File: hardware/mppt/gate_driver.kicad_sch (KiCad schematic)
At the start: 26 parts, among them Q1001 BSS127S, U1001 ADUM4221-1ARIZ

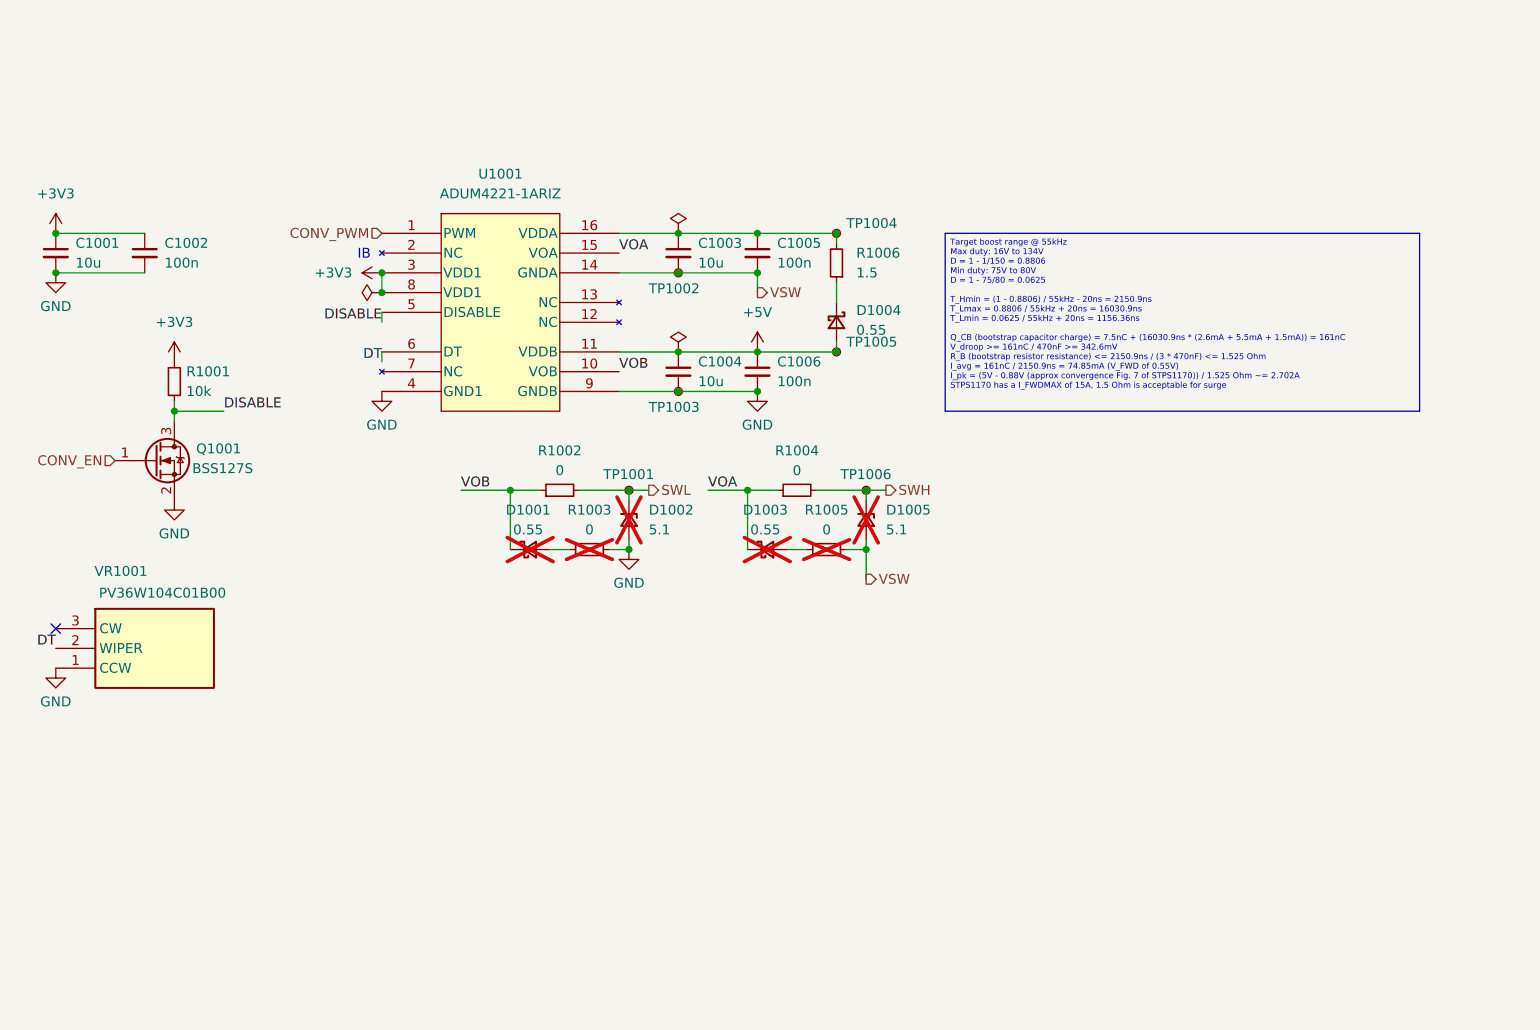
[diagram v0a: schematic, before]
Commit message: run through mppt sch, going through bom
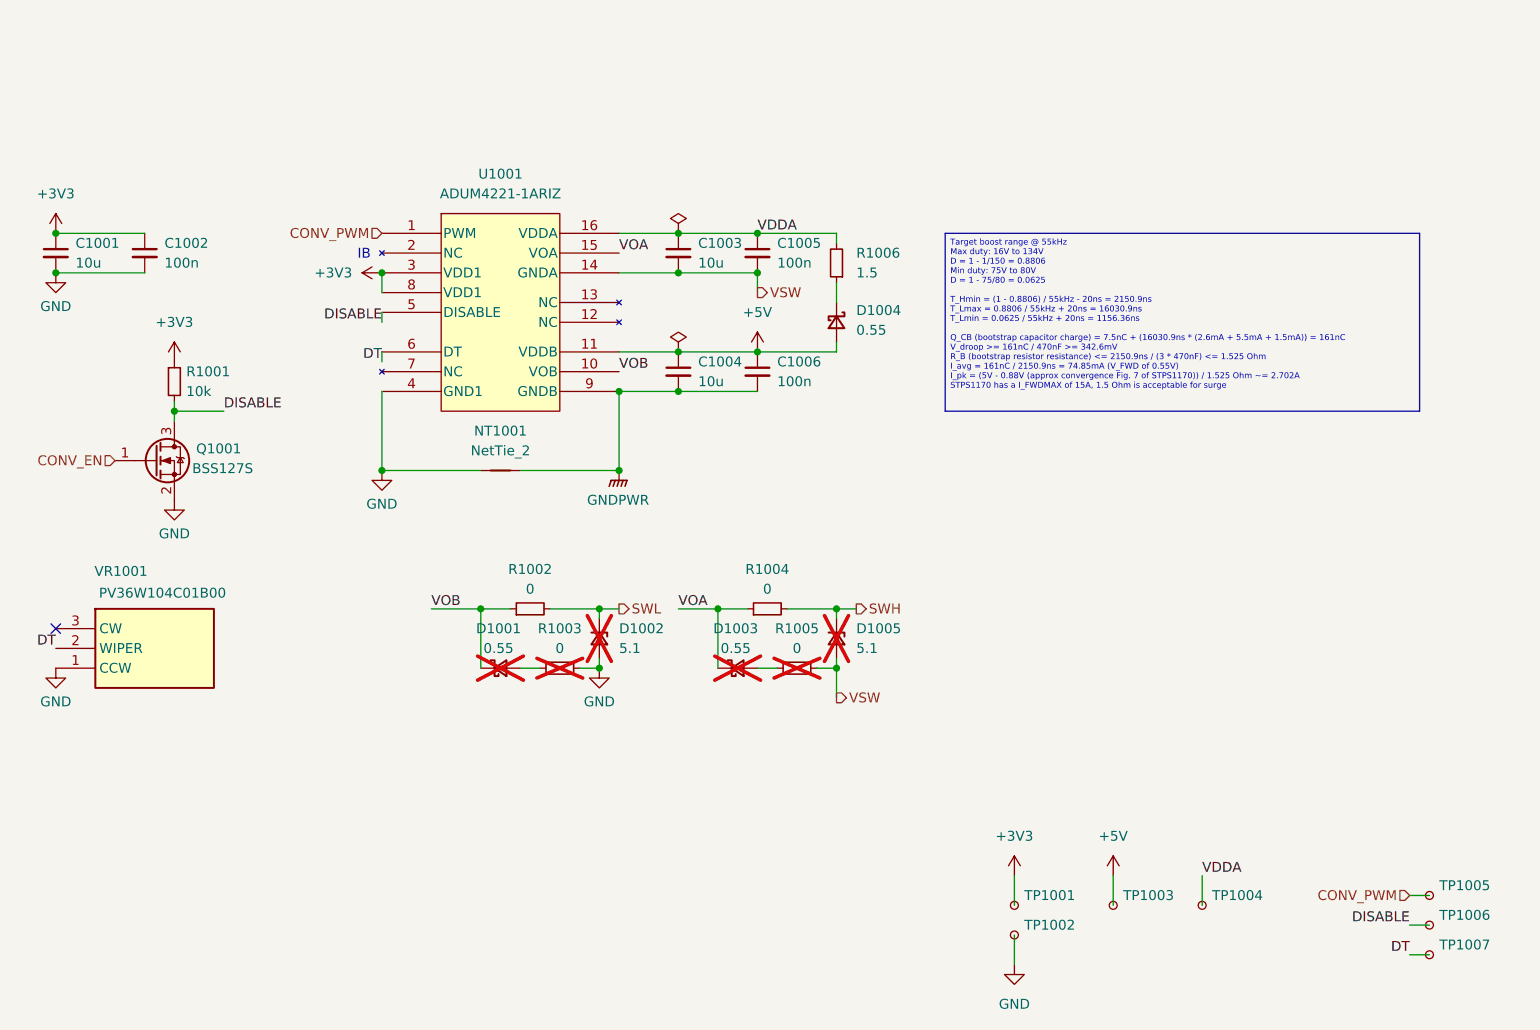
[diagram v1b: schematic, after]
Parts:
- added NT1001: NetTie_2, symbol Device:NetTie_2
- added TP1007: TestPoint_Small, symbol Connector:TestPoint_Small
- C1001: footprint Capacitor_SMD:C_0805_2012Metric_Pad1.18x1.45mm_HandSolder -> (none); Notes (none) -> 3.3V Rating; P/N CL21B106KOQNNNE -> (none)
- C1002: footprint Capacitor_SMD:C_0805_2012Metric_Pad1.18x1.45mm_HandSolder -> (none); Notes (none) -> 3.3V Rating; P/N CL21B104KCFNNNE -> (none)
- C1003, C1004: footprint Capacitor_SMD:C_0805_2012Metric_Pad1.18x1.45mm_HandSolder -> (none); Notes (none) -> 10V Rating; P/N CL21B106KOQNNNE -> (none)
- C1005, C1006: footprint Capacitor_SMD:C_0805_2012Metric_Pad1.18x1.45mm_HandSolder -> (none); Notes (none) -> 10V Rating; P/N CL21B104KCFNNNE -> (none)
- D1001, D1003, D1004: footprint footprints:stm_STPS1170AF -> (none); Manufacturer STMicrolectronics -> (none); P/N STPS1170AF -> (none)
- D1002, D1005: footprint Diode_SMD:D_SOD-123 -> (none); Manufacturer Vishay Electronics -> (none); P/N BZT52C5V1-G3-08 -> (none)
- Q1001: footprint Package_TO_SOT_SMD:SOT-23 -> (none); Manufacturer Diodes Incorporated -> (none); P/N BSS127S-7 -> (none)
- R1001: footprint Resistor_SMD:R_0805_2012Metric_Pad1.20x1.40mm_HandSolder -> (none); P/N CRCW080510K0FKEA -> (none)
- R1002, R1003, R1004, R1005: footprint Resistor_SMD:R_0805_2012Metric_Pad1.20x1.40mm_HandSolder -> (none); P/N CRCW08050000Z0EA -> (none)
- R1006: footprint Resistor_SMD:R_0805_2012Metric_Pad1.20x1.40mm_HandSolder -> (none); P/N CRCW08051R50FKEA -> (none)
- TP1001, TP1002: footprint TestPoint:TestPoint_Keystone_5000-5004_Miniature -> TestPoint:TestPoint_Pad_D1.0mm; Manufacturer Keystone Electronics -> (none); P/N 5000 -> (none)
- TP1003, TP1004, TP1005, TP1006: footprint TestPoint:TestPoint_Keystone_5000-5004_Miniature -> (none); Manufacturer Keystone Electronics -> (none); P/N 5000 -> (none)
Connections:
- net +3V3: now also TP1001.1
- net +5V: now also TP1003.1; no longer TP1005.1
- net CONV_PWM: now also TP1005.1
- net DISABLE: now also TP1006.1
- net DT: now also TP1007.1
- net GND: now also TP1002.1, NT1001.1; no longer C1004.2, C1006.2, TP1003.1, U1001.9 (GNDB)
- net SWH: no longer TP1006.1
- net SWL: no longer TP1001.1
- net VSW: no longer TP1002.1
- net VDDA: now reaches C1003.1, C1005.1, R1006.2, TP1004.1, U1001.16 (VDDA)
- new net GNDPWR: C1004.2, C1006.2, NT1001.2, U1001.9 (GNDB)
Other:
- moved on the sheet: D1001, D1002, D1003, D1005, R1002, R1003, R1004, R1005

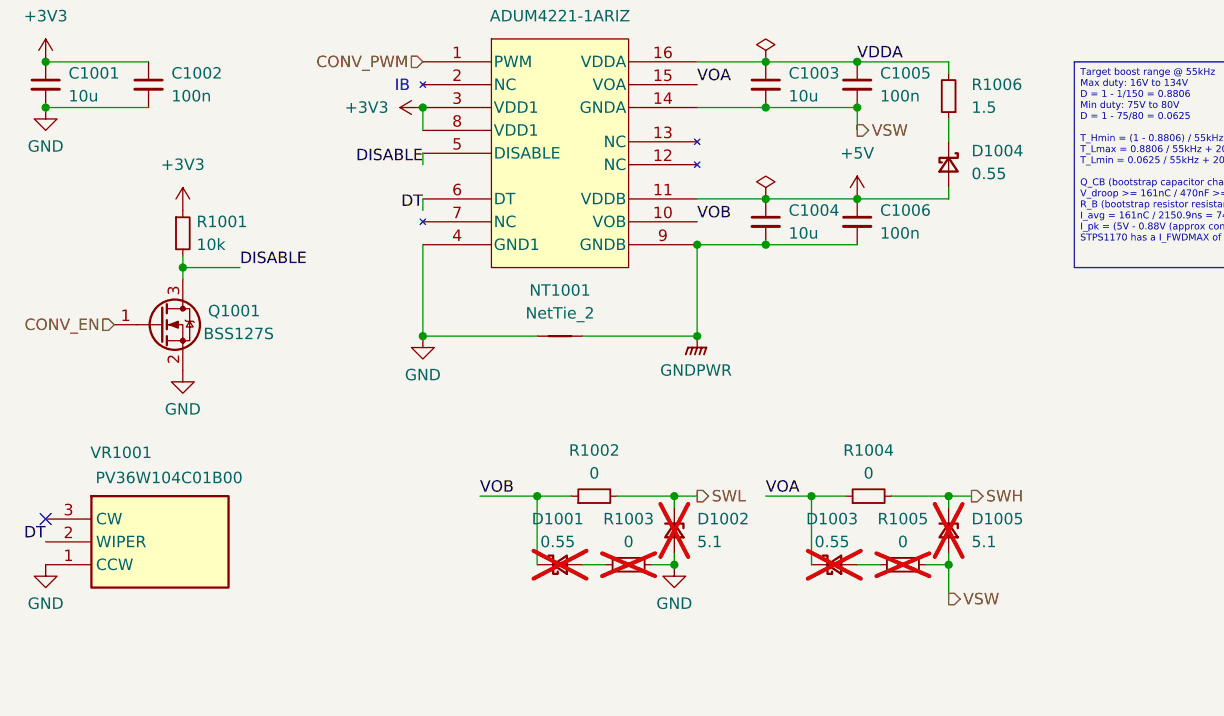
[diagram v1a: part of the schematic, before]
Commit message: update final missing pieces for sch, moving to bom pop
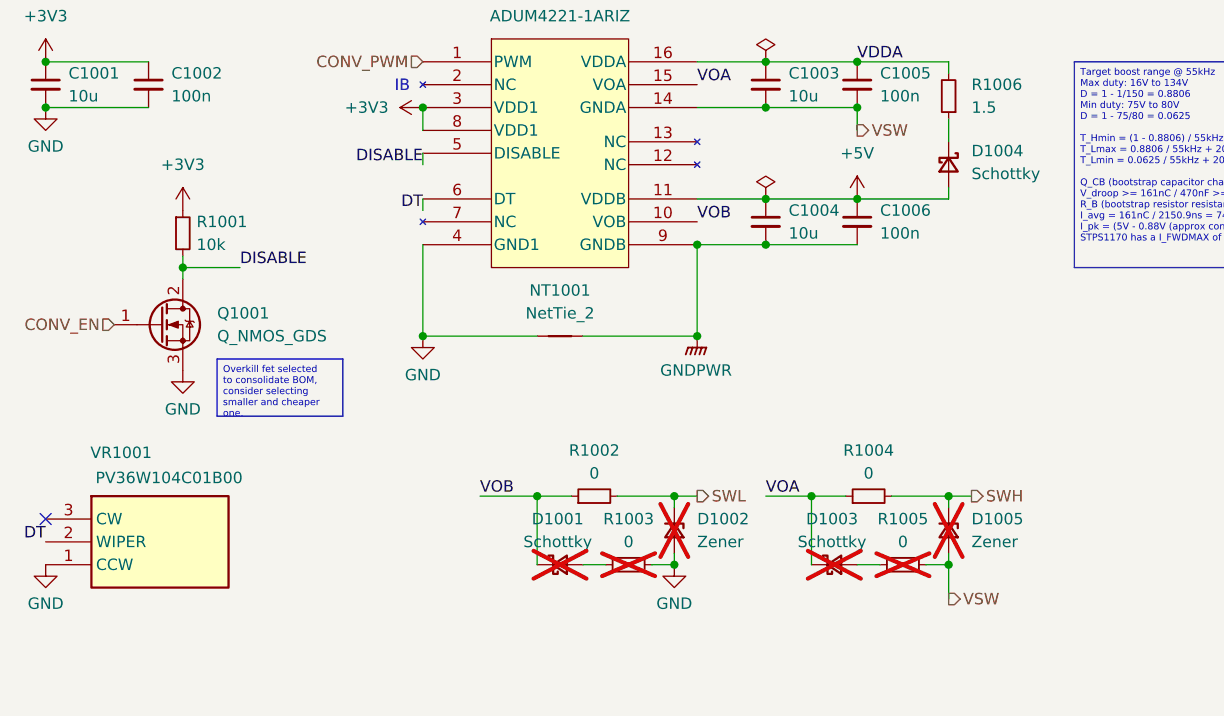
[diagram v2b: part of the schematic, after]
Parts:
- removed Q1001: BSS127S, symbol Transistor_FET:BSS127S
- added Q1001: Q_NMOS_GDS, Package_TO_SOT_SMD:SOT-223-3_TabPin2, symbol Device:Q_NMOS_GDS
- D1001, D1003, D1004: value 0.55 -> Schottky; Notes (none) -> 0.55 Forward
- D1002, D1005: value 5.1 -> Zener; Notes (none) -> 5.1V Standoff
- NT1001: footprint (none) -> NetTie:NetTie-2_SMD_Pad2.0mm
- R1001, R1002, R1003, R1004, R1005, R1006: Manufacturer Vishay Dale -> Vishay / Dale
- TP1003, TP1004, TP1005, TP1006, TP1007: footprint (none) -> TestPoint:TestPoint_Pad_D1.0mm
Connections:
- net CONV_EN: now also Q1001.1 (G)
- net DISABLE: now also Q1001.2 (D)
- net GND: now also Q1001.3 (S)
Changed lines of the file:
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@@
 		)
 	)
+	(text_box "Overkill fet selected to consolidate BOM, \nconsider selecting smaller and cheaper one."
+		(exclude_from_sim no)
+		(at 69.85 96.52 0)
+		(size 13.97 6.35)
+		(stroke
+			(width 0)
+			(type default)
+		)
+		(fill
+			(type none)
+		)
+		(effects
+			(font
+				(size 0.762 0.762)
+			)
+			(justify left top)
+		)
+	)
 	(text_box "Target boost range @ 55kHz\nMax duty: 16V to 134V\nD = 1 - 1/150 = 0.8806\nMin duty: 75V to 80V \nD = 1 - 75/80 = 0.0625\n\nT_Hmin = (1 - 0.8806) / 55kHz - 20ns = 2150.9ns\nT_Lmax = 0.8806 / 55kHz + 20ns = 16030.9ns\nT_Lmin = 0.0625 / 55kHz + 20ns = 1156.36ns\n\nQ_CB (bootstrap capacitor charge) = 7.5nC + (16030.9ns * (2.6mA + 5.5mA + 1.5mA)) = 161nC\nV_droop >= 161nC / 470nF >= 342.6mV\nR_B (bootstrap resistor resistance) <= 2150.9ns / (3 * 470nF) <= 1.525 Ohm\nI_avg = 161nC / 2150.9ns = 74.85mA (V_FWD of 0.55V)\nI_pk = (5V - 0.88V (approx convergence Fig. 7 of STPS1170)) / 1.525 Ohm ~= 2.702A\nSTPS1170 has a I_FWDMAX of 15A, 1.5 Ohm is acceptable for surge\n"
 		(exclude_from_sim no)
@@
 			)
 		)
-		(property "Manufacturer" "Vishay Dale"
+		(property "Manufacturer" "Vishay / Dale"
 			(at 151.13 67.31 0)
 			(effects
@@
 			)
 		)
-		(property "Manufacturer" "Vishay Dale"
+		(property "Manufacturer" "Vishay / Dale"
 			(at 66.04 82.55 0)
 			(effects
@@
 			)
 		)
-		(property "Manufacturer" "Vishay Dale"
+		(property "Manufacturer" "Vishay / Dale"
 			(at 146.05 119.38 90)
 			(effects
@@
 			)
 		)
-		(property "Manufacturer" "Vishay Dale"
+		(property "Manufacturer" "Vishay / Dale"
 			(at 111.76 111.76 90)
 			(effects
@@
 			)
 		)
-		(property "Value" "5.1"
+		(property "Value" "Zener"
 			(at 153.67 116.8399 90)
 			(effects
@@
 			)
 		)
-		(property "Notes" ""
+		(property "Notes" "5.1V  Standoff"
 			(at 151.13 115.57 0)
 			(effects
@@
 			)
 		)
-		(property "Manufacturer" "Vishay Dale"
+		(property "Manufacturer" "Vishay / Dale"
 			(at 115.57 119.38 90)
 			(effects
@@
 			)
 		)
-		(property "Footprint" ""
+		(property "Footprint" "NetTie:NetTie-2_SMD_Pad2.0mm"
 			(at 107.95 93.98 0)
 			(effects
@@
 			)
 		)
-		(property "Datasheet" "~"
+		(property "Datasheet" ""
 			(at 107.95 93.98 0)
 			(effects
@@
 			)
 		)
-		(property "Footprint" ""
+		(property "Footprint" "TestPoint:TestPoint_Pad_D1.0mm"
 			(at 232.41 152.4 0)
 			(effects
@@
 			)
 		)
-		(property "Value" "5.1"
+		(property "Value" "Zener"
 			(at 123.19 116.8399 90)
 			(effects
@@
 			)
 		)
-		(property "Notes" ""
+		(property "Notes" "5.1V  Standoff"
 			(at 120.65 115.57 0)
 			(effects
@@
 			)
 		)
-		(property "Value" "0.55"
+		(property "Value" "Schottky"
 			(at 107.696 116.84 0)
 			(effects
@@
 			)
 		)
-		(property "Notes" ""
+		(property "Notes" "0.55 Forward"
 			(at 107.95 119.38 90)
 			(effects
@@
 			)
 		)
-		(property "Value" "0.55"
+		(property "Value" "Schottky"
 			(at 153.67 75.9459 90)
 			(effects
@@
 			)
 		)
-		(property "Notes" ""
+		(property "Notes" "0.55 Forward"
 			(at 151.13 74.93 90)
 			(effects
@@
 			)
 		)
-		(property "Footprint" ""
+		(property "Footprint" "TestPoint:TestPoint_Pad_D1.0mm"
 			(at 203.2 149.86 0)
 			(effects
@@
 			)
 		)
-		(property "Footprint" ""
+		(property "Footprint" "TestPoint:TestPoint_Pad_D1.0mm"
 			(at 232.41 148.59 0)
 			(effects
@@
 			)
 		)
-		(property "Value" "0.55"
+		(property "Value" "Schottky"
 			(at 138.176 116.84 0)
 			(effects
@@
 			)
 		)
-		(property "Notes" ""
+		(property "Notes" "0.55 Forward"
 			(at 138.43 119.38 90)
 			(effects
@@
 			)
 		)
-		(property "Footprint" ""
+		(property "Footprint" "TestPoint:TestPoint_Pad_D1.0mm"
 			(at 232.41 156.21 0)
 			(effects
@@
 			)
 		)
-		(property "Footprint" ""
+		(property "Footprint" "TestPoint:TestPoint_Pad_D1.0mm"
 			(at 191.77 149.86 0)
 			(effects
@@
 	)
 	(symbol
-		(lib_id "Transistor_FET:BSS127S")
-		(at 63.5 92.71 0)
-		(unit 1)
-		(exclude_from_sim no)
-		(in_bom yes)
-		(on_board yes)
-		(dnp no)
-		(property "Reference" "Q1001"
-			(at 68.834 91.186 0)
-			(effects
-				(font
-					(size 1.27 1.27)
-				)
-				(justify left)
-			)
-		)
-		(property "Value" "BSS127S"
-			(at 68.326 93.726 0)
-			(effects
-				(font
-					(size 1.27 1.27)
-				)
-				(justify left)
-			)
-		)
-		(property "Footprint" ""
-			(at 68.58 94.615 0)
-			(effects
-				(font
-					(size 1.27 1.27)
-					(italic yes)
-				)
-				(justify left)
-				(hide yes)
-			)
-		)
-		(property "Datasheet" ""
-			(at 68.58 96.52 0)
-			(effects
-				(font
-					(size 1.27 1.27)
-				)
-				(justify left)
-				(hide yes)
-			)
-		)
-		(property "Description" "0.07A Id, 600V Vds, N-Channel MOSFET, SOT-23"
-			(at 63.5 92.71 0)
-			(effects
-				(font
-					(size 1.27 1.27)
-				)
-				(hide yes)
-			)
-		)
-		(property "Cost" ""
-			(at 63.5 92.71 0)
-			(effects
-				(font
-					(size 1.27 1.27)
-				)
-				(hide yes)
-			)
-		)
-		(property "Distributor" ""
-			(at 63.5 92.71 0)
-			(effects
-				(font
-					(size 1.27 1.27)
-				)
-				(hide yes)
-			)
-		)
-		(property "Manufacturer" ""
-			(at 63.5 92.71 0)
-			(effects
-				(font
-					(size 1.27 1.27)
-				)
-				(hide yes)
-			)
-		)
-		(property "Notes" ""
-			(at 63.5 92.71 0)
-			(effects
-				(font
-					(size 1.27 1.27)
-				)
-				(hide yes)
-			)
-		)
-		(property "P/N" ""
-			(at 63.5 92.71 0)
-			(effects
-				(font
-					(size 1.27 1.27)
-				)
-				(hide yes)
-			)
-		)
-		(property "Sim.Device" ""
-			(at 63.5 92.71 0)
-			(effects
-				(font
-					(size 1.27 1.27)
-				)
-				(hide yes)
-			)
-		)
-		(property "Sim.Pins" ""
-			(at 63.5 92.71 0)
-			(effects
-				(font
-					(size 1.27 1.27)
-				)
-				(hide yes)
-			)
-		)
-		(pin "3"
-		)
-		(pin "1"
-		)
-		(pin "2"
-		)
-		(instances
-			(project "mppt"
-				(path "/83ad0d2f-976b-4ec4-beba-98e6b6988069/1e7e948a-199f-4420-b7b6-1130e9474bfe/6fd27594-6b47-4401-bb7d-37a86a40ba18"
-					(reference "Q1001")
-					(unit 1)
-				)
-			)
-		)
-	)
-	(symbol
 		(lib_id "power:GND")
 		(at 173.99 157.48 0)
@@
 			)
 		)
-		(property "Manufacturer" "Vishay Dale"
+		(property "Manufacturer" "Vishay / Dale"
 			(at 142.24 111.76 90)
 			(effects
@@
 					(unit 1)
 				)
+			)
+		)
+	)
+	(symbol
+		(lib_id "Device:Q_NMOS_GDS")
+		(at 63.5 92.71 0)
+		(unit 1)
+		(exclude_from_sim no)
+		(in_bom yes)
+		(on_board yes)
+		(dnp no)
+		(fields_autoplaced yes)
+		(property "Reference" "Q1001"
+			(at 69.85 91.4399 0)
+			(effects
+				(font
+					(size 1.27 1.27)
+				)
+				(justify left)
+			)
+		)
+		(property "Value" "Q_NMOS_GDS"
+			(at 69.85 93.9799 0)
+			(effects
+				(font
+					(size 1.27 1.27)
+				)
+				(justify left)
+			)
+		)
+		(property "Footprint" "Package_TO_SOT_SMD:SOT-223-3_TabPin2"
+			(at 68.58 90.17 0)
+			(effects
+				(font
+					(size 1.27 1.27)
+				)
+				(hide yes)
+			)
+		)
+		(property "Datasheet" "~"
+			(at 63.5 92.71 0)
+			(effects
+				(font
+					(size 1.27 1.27)
+				)
+				(hide yes)
+			)
+		)
+		(property "Description" "N-MOSFET transistor, gate/drain/source"
+			(at 63.5 92.71 0)
+			(effects
+				(font
+					(size 1.27 1.27)
+				)
+				(hide yes)
+			)
+		)
+		(property "Distributor" ""
+			(at 63.5 92.71 0)
+			(effects
+				(font
+					(size 1.27 1.27)
+				)
+				(hide yes)
+			)
+		)
+		(property "Manufacturer" "Infineon"
+			(at 63.5 92.71 0)
+			(effects
+				(font
+					(size 1.27 1.27)
+				)
+				(hide yes)
+			)
+		)
+		(property "P/N" "BSP297H6327"
+			(at 63.5 92.71 0)
+			(effects
+				(font
+					(size 1.27 1.27)
+				)
+				(hide yes)
+			)
+		)
+		(property "LCSC Part #" ""
+			(at 63.5 92.71 0)
+			(effects
+				(font
+					(size 1.27 1.27)
+				)
+				(hide yes)
+			)
+		)
+		(property "Cost" ""
+			(at 63.5 92.71 0)
+			(effects
+				(font
+					(size 1.27 1.27)
+				)
+				(hide yes)
+			)
+		)
+		(property "Notes" ""
+			(at 63.5 92.71 0)
+			(effects
+				(font
+					(size 1.27 1.27)
+				)
+				(hide yes)
+			)
+		)
+		(pin "3"
+		)
+		(pin "2"
+		)
+		(pin "1"
+		)
+		(instances
+			(project "mppt"
+				(path "/83ad0d2f-976b-4ec4-beba-98e6b6988069/1e7e948a-199f-4420-b7b6-1130e9474bfe/6fd27594-6b47-4401-bb7d-37a86a40ba18"
+					(reference "Q1001")
+					(unit 1)
+				)

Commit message: bom consolidated, starting layout
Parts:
- C1001, C1003, C1004: footprint (none) -> Capacitor_SMD:C_1206_3216Metric_Pad1.33x1.80mm_HandSolder; Manufacturer Samsung Electro-Mechanics -> TDK; P/N (none) -> CGA5L1X7R1E106K160AC
- C1002, C1005, C1006: footprint (none) -> Capacitor_SMD:C_0402_1005Metric_Pad0.74x0.62mm_HandSolder; Manufacturer Samsung Electro-Mechanics -> TDK; P/N (none) -> CGA2B3X7R1H104K050BB
- D1001, D1003, D1004: footprint (none) -> Diode_SMD:D_SOD-123F; Manufacturer (none) -> Diodes Incorporated; Notes 0.55 Forward -> (none); P/N (none) -> SBR3U40S1F-7
- D1002, D1005: footprint (none) -> Diode_SMD:D_SOD-123F; Manufacturer (none) -> Diodes Incorporated; P/N (none) -> BZT52HC5V1WF-7
- NT1001: footprint NetTie:NetTie-2_SMD_Pad2.0mm -> NetTie:NetTie-2_SMD_Pad0.5mm
- R1001: footprint (none) -> Resistor_SMD:R_0603_1608Metric_Pad0.98x0.95mm_HandSolder; P/N (none) -> CRCW060310K0FKEA
- R1002, R1003, R1004, R1005: footprint (none) -> Resistor_SMD:R_1210_3225Metric_Pad1.30x2.65mm_HandSolder; P/N (none) -> CRCW12100000Z0EA
- R1006: footprint (none) -> Resistor_SMD:R_1210_3225Metric_Pad1.30x2.65mm_HandSolder; P/N (none) -> CRCW12101R50JNEA
